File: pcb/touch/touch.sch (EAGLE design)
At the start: 18 parts, among them U1 MPR084EJ

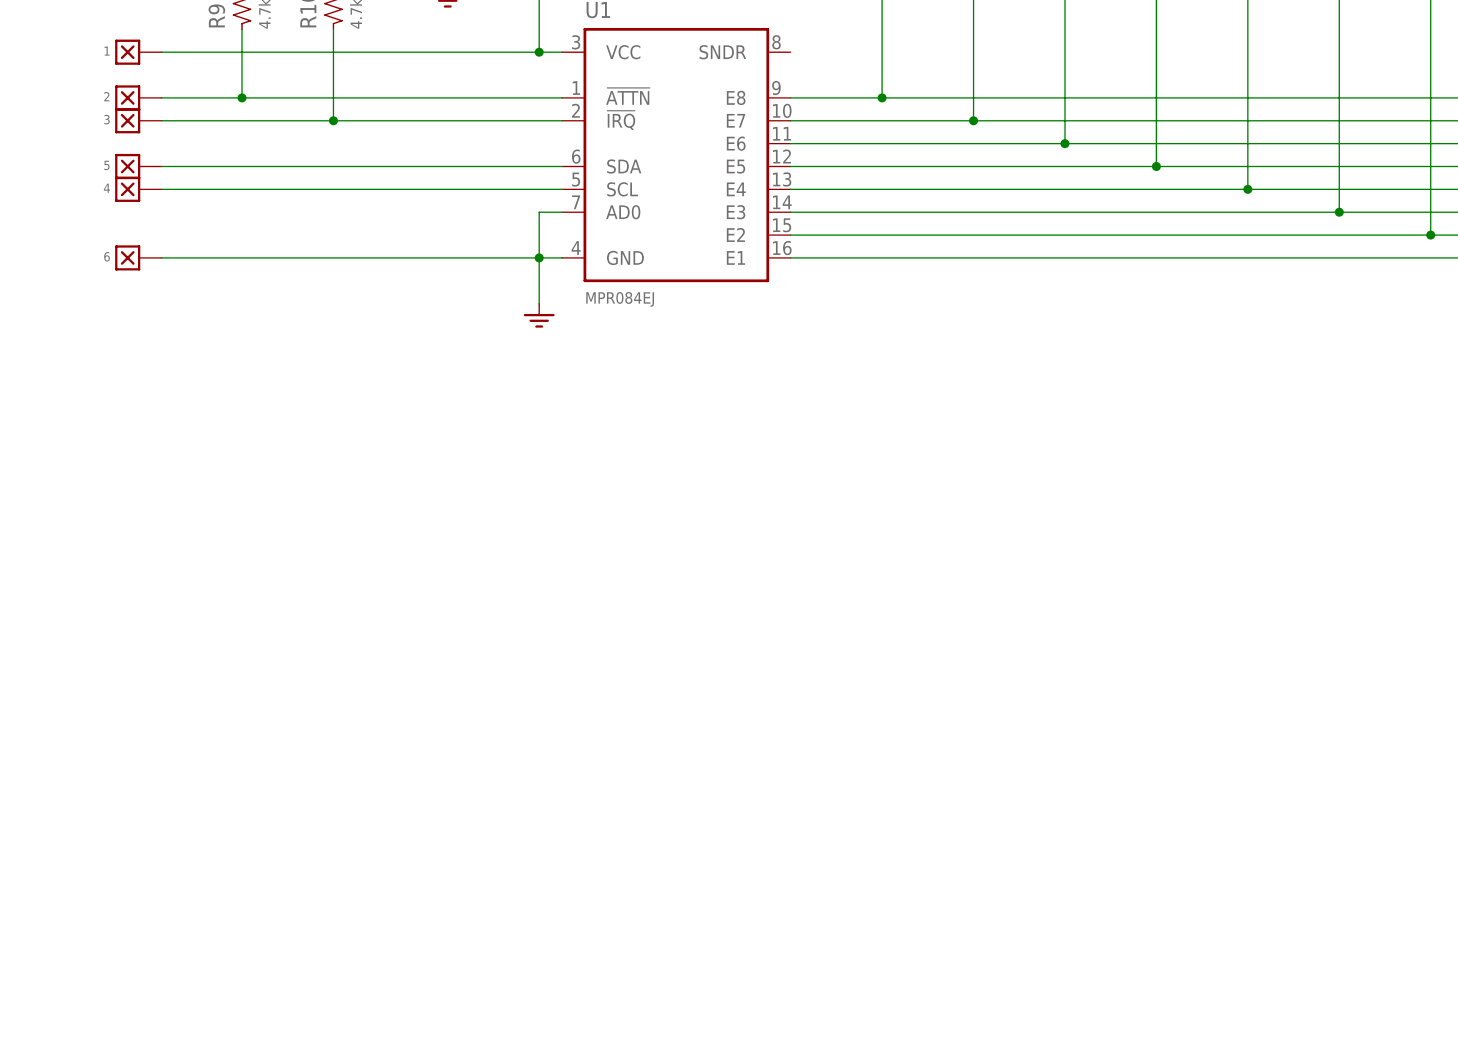
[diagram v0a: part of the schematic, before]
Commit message: Corrected drawings of touch panel PCB
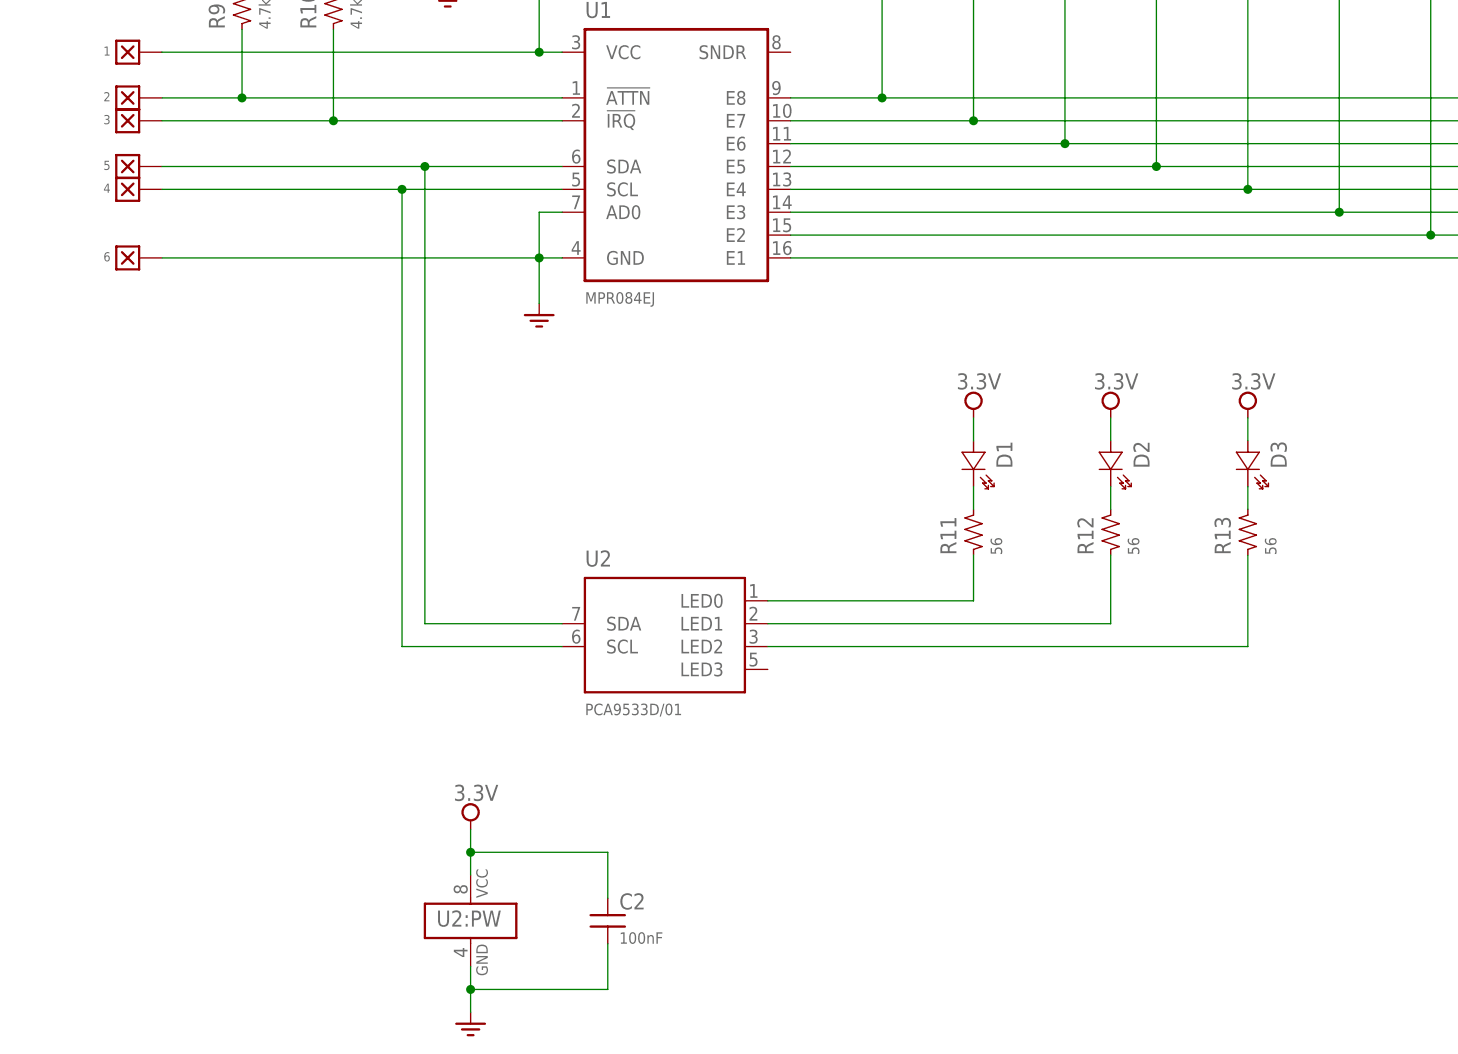
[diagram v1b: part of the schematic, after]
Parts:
- added C2: 100nF, Passive:CAP-0603
- added D1, D2, D3: {ATTR:COLOR}, Optoelectronic:LED-0805
- added R11, R12, R13: 56, Passive:RES-0603
- added U2: PCA9533D/01, IC:PCA9533D/01
- !ATTN, !IRQ, 3.3V, SCL, SDA, W6: NO_BOM 1 -> (none)
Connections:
- new net N$1: D1.K, R11.2
- new net N$2: D2.K, R12.2
- new net N$3: D3.K, R13.2
- new net N$4: R11.1, U2G$1.LED0
- new net N$5: R12.1, U2G$1.LED1
- new net N$6: R13.1, U2G$1.LED2
- net 3.3V: now also C2.1, D1.A, D2.A, D3.A, U2:PW.VCC
- net GND: now also C2.2, U2:PW.GND
- net SCL: now also U2G$1.SCL
- net SDA: now also U2G$1.SDA

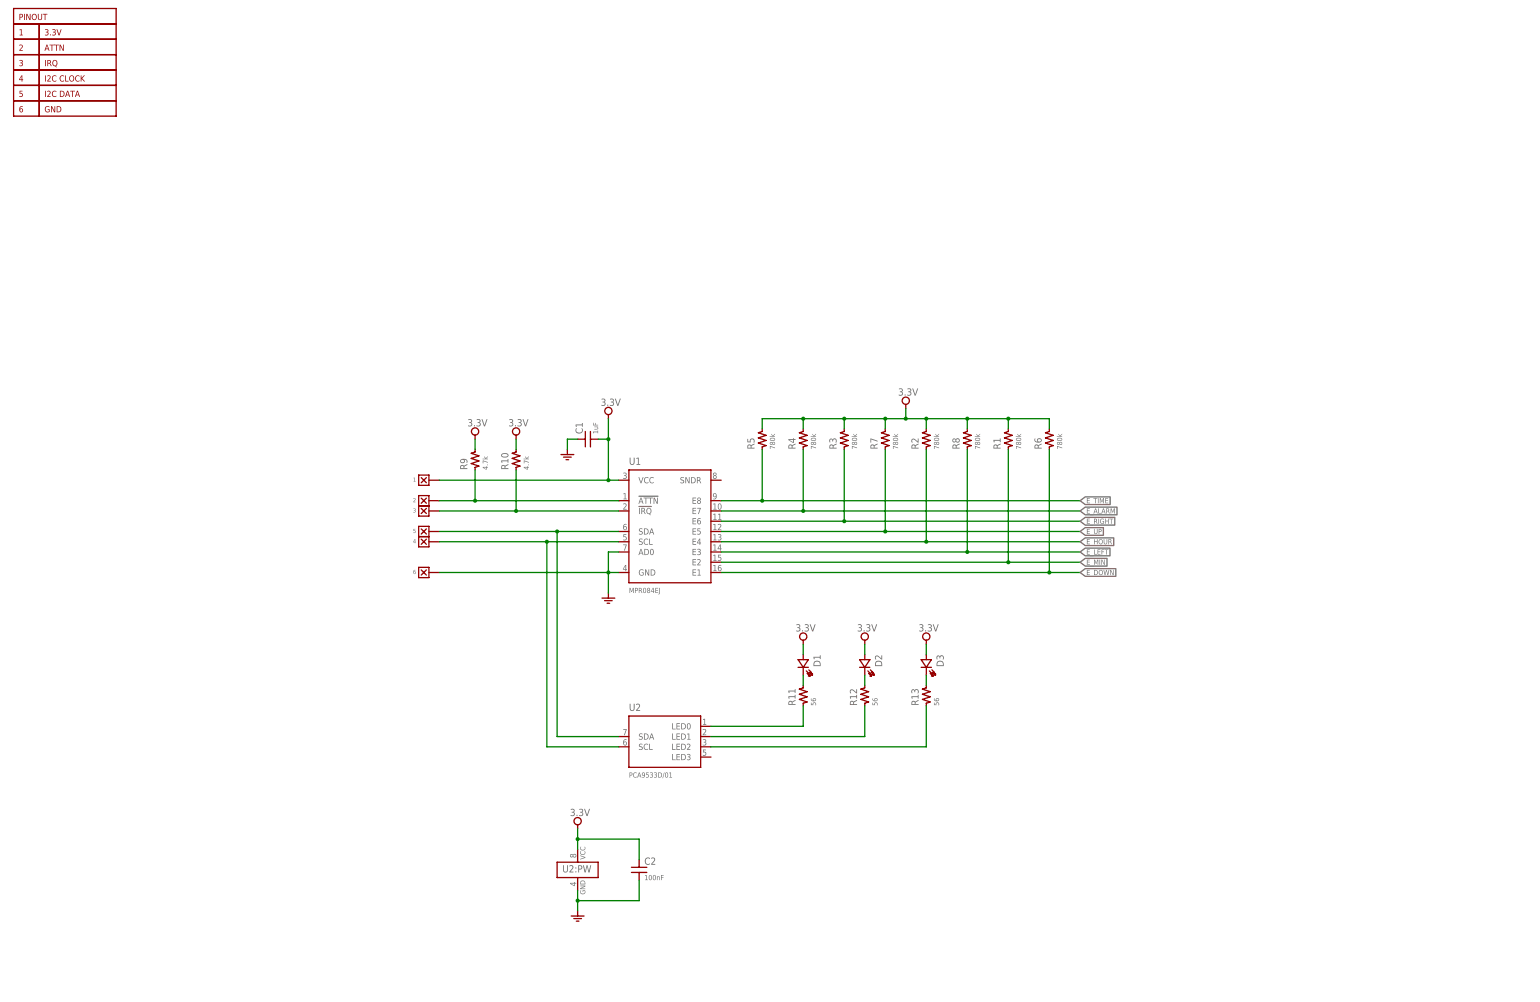
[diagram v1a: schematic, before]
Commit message: Display base pcb (rev C), Touch panel (rev B)
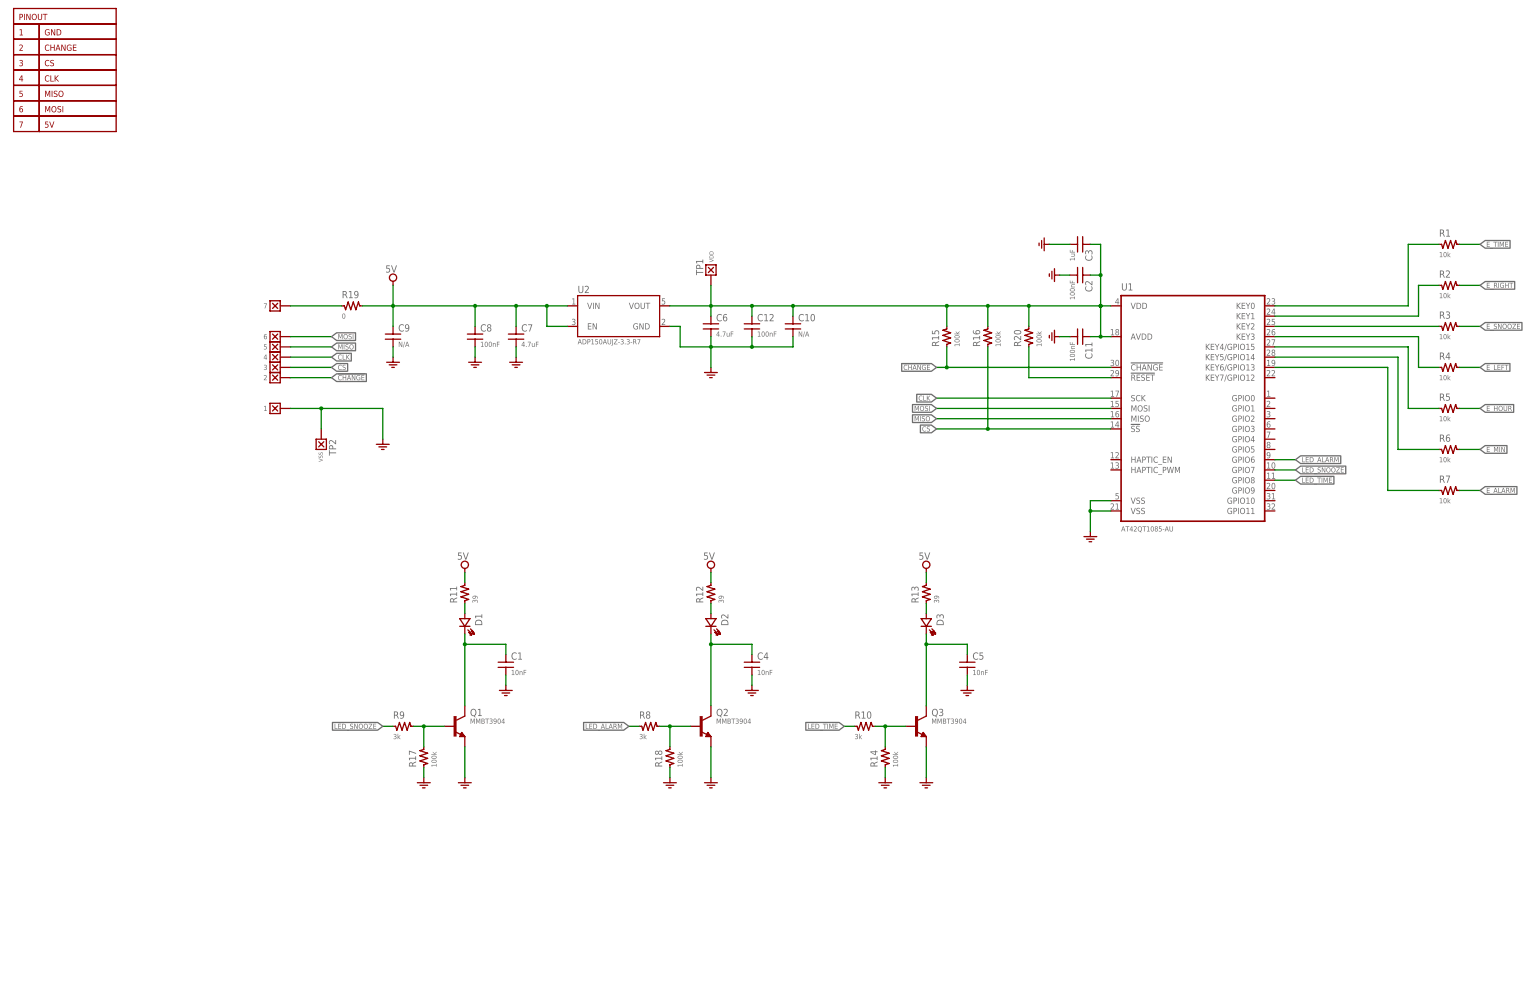
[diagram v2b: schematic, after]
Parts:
- removed !ATTN: 2, Misc:WIRE
- removed !IRQ: 3, Misc:WIRE
- removed 3.3V: 1, Misc:WIRE
- removed SCL: 4, Misc:WIRE
- removed SDA: 5, Misc:WIRE
- removed W6: 6, Misc:WIRE
- added !CHANGE: 2, Misc:WIRE-125X50
- added 5V: 7, Misc:WIRE-150X75
- added C10, C9: N/A, Passive:CAP-1206
- added C11, C12, C8: 100nF, Passive:CAP-0603
- added C3: 1uF, Passive:CAP-1206
- added C4, C5: 10nF, Passive:CAP-0603
- added C6, C7: 4.7uF, Passive:CAP-1206
- added CLK: 4, Misc:WIRE-125X50
- added CS: 3, Misc:WIRE-125X50
- added GND: 1, Misc:WIRE-150X75
- added MISO: 5, Misc:WIRE-125X50
- added MOSI: 6, Misc:WIRE-125X50
- added Q1, Q2, Q3: MMBT3904, Transistor:MMBT3904
- added R14, R15, R16, R17, R18, R20: 100k, Passive:RES-0603
- added R19: 0, Passive:RES-1206
- added TP1: VDD, Misc:TEST_POINT-050
- added TP2: VSS, Misc:TEST_POINT-050
- C1: value 1uF -> 10nF
- D1, D2, D3: device Optoelectronic:LED-0805 -> Optoelectronic:LR-P47F; COLOR (none) -> Red; DESCRIPTION (none) -> {DESCRIPTION} - Red
- R1: value 780k -> 10k; DESCRIPTION {DESCRIPTION} - SMT 0603 - {VALUE} -> (none); PACKAGE SMT 0603 -> (none)
- R10: value 4.7k -> 3k; DESCRIPTION {DESCRIPTION} - SMT 0603 - {VALUE} -> (none); PACKAGE SMT 0603 -> (none)
- R11, R12, R13: value 56 -> 39
- R2, R3, R4, R5, R6, R7: value 780k -> 10k
- R8: value 780k -> 3k; DESCRIPTION {DESCRIPTION} - SMT 0603 - {VALUE} -> (none); PACKAGE SMT 0603 -> (none)
- R9: value 4.7k -> 3k
- U1: value MPR084EJ -> AT42QT1085-AU; device IC:MPR084EJ -> IC:AT42QT1085-AU
- U2: value PCA9533D/01 -> ADP150AUJZ-3.3-R7; device IC:PCA9533D/01 -> Power:ADP150AUJZ-3.3-R7; DESCRIPTION (none) -> {DESCRIPTION} - 3.3v
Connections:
- removed net !ATTN: !ATTN.P$1, R9.1, U1.!ATTN
- removed net !IRQ: !IRQ.P$1, R10.1, U1.!IRQ
- removed net 3.3V: 3.3V.P$1, C1.2, C2.1, D1.A, D2.A, D3.A, R1.2, R10.2, R2.2, R3.2, R4.2, R5.2, R6.2, R7.2, R8.2, R9.2, U1.VCC, U2:PW.VCC
- removed net E_DOWN: R6.1, U1.E1
- removed net E_UP: R7.1, U1.E5
- removed net SCL: SCL.P$1, U1.SCL, U2G$1.SCL
- removed net SDA: SDA.P$1, U1.SDA, U2G$1.SDA
- new net !CHANGE: !CHANGE.P$1, R15.1, U1.!CHANGE
- new net 5V: C7.1, C8.1, C9.1, R11.2, R12.2, R13.2, R19.2, U2.EN, U2.VIN
- new net CLK: CLK.P$1, U1.SCK
- new net CS: CS.P$1, R16.1, U1.!SS
- new net E_SNOOZE: R3.2
- new net LED_ALARM: R8.1, U1.GPIO6
- new net LED_SNOOZE: R9.1, U1.GPIO7
- new net LED_TIME: R10.1, U1.GPIO8
- new net MISO: MISO.P$1, U1.MISO
- new net MOSI: MOSI.P$1, U1.MOSI
- new net N$10: R4.1, U1.KEY3
- new net N$11: R5.1, U1.KEY4/GPIO15
- new net N$12: R6.1, U1.KEY5/GPIO14
- new net N$13: R7.1, U1.KEY6/GPIO13
- new net N$14: Q3.B, R10.2, R14.2
- new net N$15: Q2.B, R18.2, R8.2
- new net N$16: Q1.B, R17.2, R9.2
- new net N$18: 5V.P$1, R19.1
- new net N$19: R20.1, U1.!RESET
- new net N$7: R1.1, U1.KEY0
- new net N$8: R2.1, U1.KEY1
- new net N$9: R3.1, U1.KEY2
- new net VDD: C10.1, C11.1, C12.1, C2.1, C3.1, C6.1, R15.2, R16.2, R20.2, TP1.P$1, U1.AVDD, U1.VDD, U2.VOUT
- net E_ALARM: now also R7.2; no longer R4.1, U1.E7
- net E_HOUR: now also R5.2; no longer R2.1, U1.E4
- net E_LEFT: now also R4.2; no longer R8.1, U1.E3
- net E_MIN: now also R6.2; no longer R1.1, U1.E2
- net E_RIGHT: now also R2.2; no longer R3.1, U1.E6
- net E_TIME: now also R1.2; no longer R5.1, U1.E8
- net GND: now also C1.2, C10.2, C11.2, C12.2, C3.2, C4.2, C5.2, C6.2, C7.2, C8.2, C9.2, GND.P$1, Q1.E, Q2.E, Q3.E, R14.1, R17.1, R18.1, TP2.P$1, U1.VSS@1, U1.VSS@2, U2.GND; no longer C1.1, U1.AD0, U1.GND, U2:PW.GND, W6.P$1
- net N$1: now also C1.1, Q1.C; no longer R11.2
- net N$2: now also C4.1, Q2.C; no longer R12.2
- net N$3: now also C5.1, Q3.C; no longer R13.2
- net N$4: now also D1.A; no longer U2G$1.LED0
- net N$5: now also D2.A; no longer U2G$1.LED1
- net N$6: now also D3.A; no longer U2G$1.LED2
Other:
- moved on the sheet: C1, C2, D1, D2, D3, R1, R10, R11, R12, R13, R2, R3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

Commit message: Changed page format on schematics to US letter (8.5" x 11")
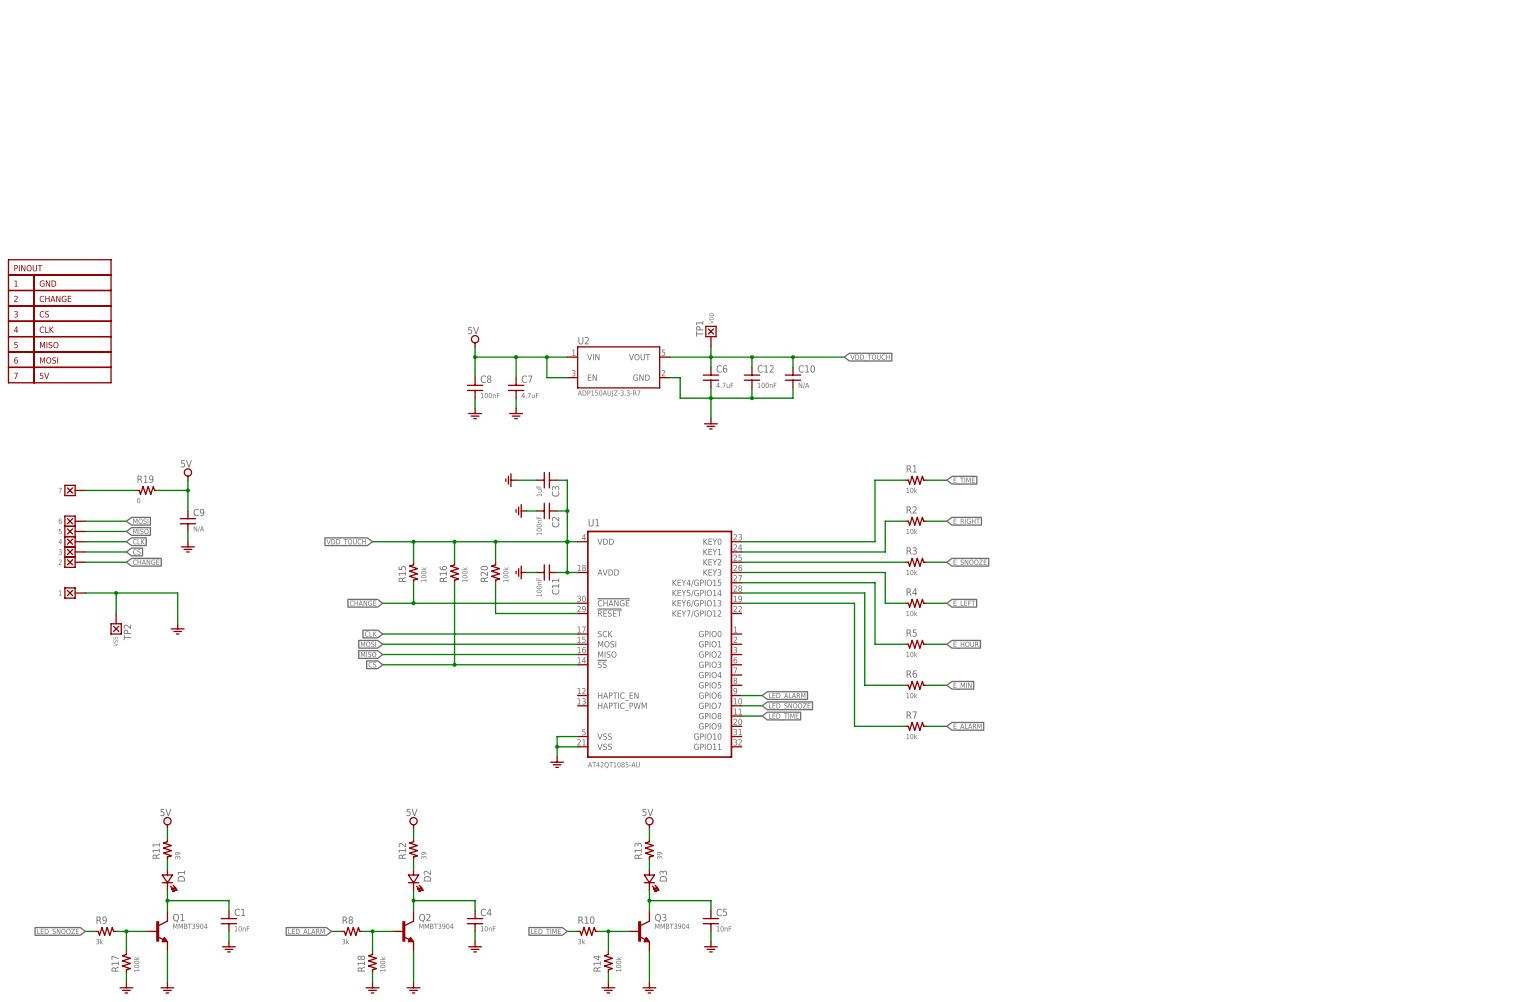
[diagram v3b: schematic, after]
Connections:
- net VDD renamed VDD_TOUCH
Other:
- moved on the sheet: C1, C10, C11, C12, C2, C3, C4, C5, C6, C7, C8, C9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
